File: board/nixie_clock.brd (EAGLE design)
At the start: 130 x 79 mm, 43 parts, among them U1 AMS1117-5.0, U2 SN74141N

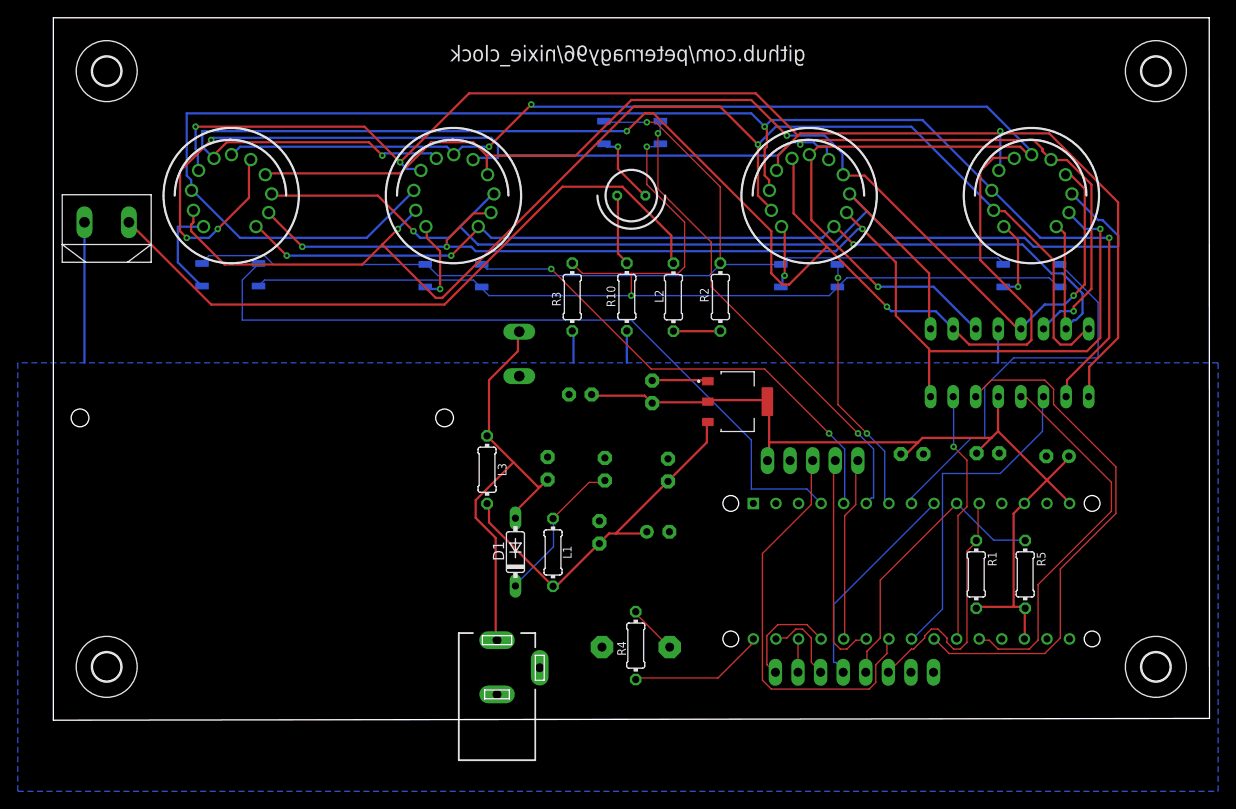
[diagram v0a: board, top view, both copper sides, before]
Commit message: D13 pin added and minor placement changes
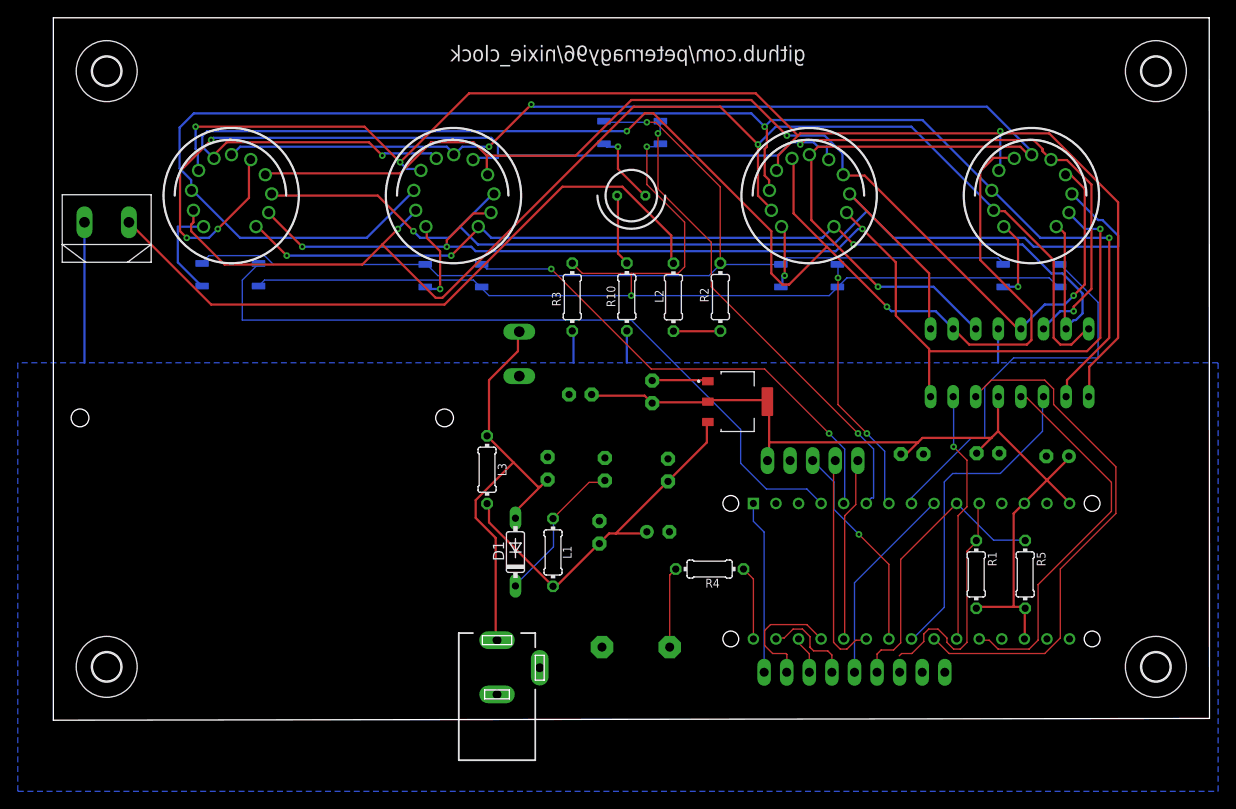
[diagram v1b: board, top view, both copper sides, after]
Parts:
- BUTTONS: device con-lstb:MA08-1 -> con-lstb:MA09-1
- moved R4 12.0 mm to (73.8, 17.0), turned to 180 degrees
- renumbered ARDUINO_NANO1 to ARDUINO_NANO
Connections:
- new net D13: ARDUINO_NANO.1, BUTTONS.9
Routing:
- net N$7: track 46.0 -> 24.1 mm, vias 0 -> 1
- net D13: track 0.00 -> 19.5 mm
- net N$8: track 15.5 -> 8.32 mm
- net D12: track 5.58 -> 9.06 mm
- net N$20: track 11.8 -> 13.9 mm
- net N$17: track 24.4 -> 22.7 mm
- net N$10: track 28.8 -> 27.2 mm
- net N$18: track 9.11 -> 10.6 mm
- net N$15: track 84.0 -> 83.0 mm
- net N$14: track 37.3 -> 36.6 mm
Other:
- board text added: "A5"
- board text added: "A6"
- board text added: "A7"
- board text added: "D10"
- board text added: "D11"
- board text added: "D13"
- board text added: "D9"
- board text removed: "b1"
- board text removed: "e"
- board text removed: "s1d"
- board text removed: "s1u"
- board text removed: "s2d"
- board text removed: "s2u"

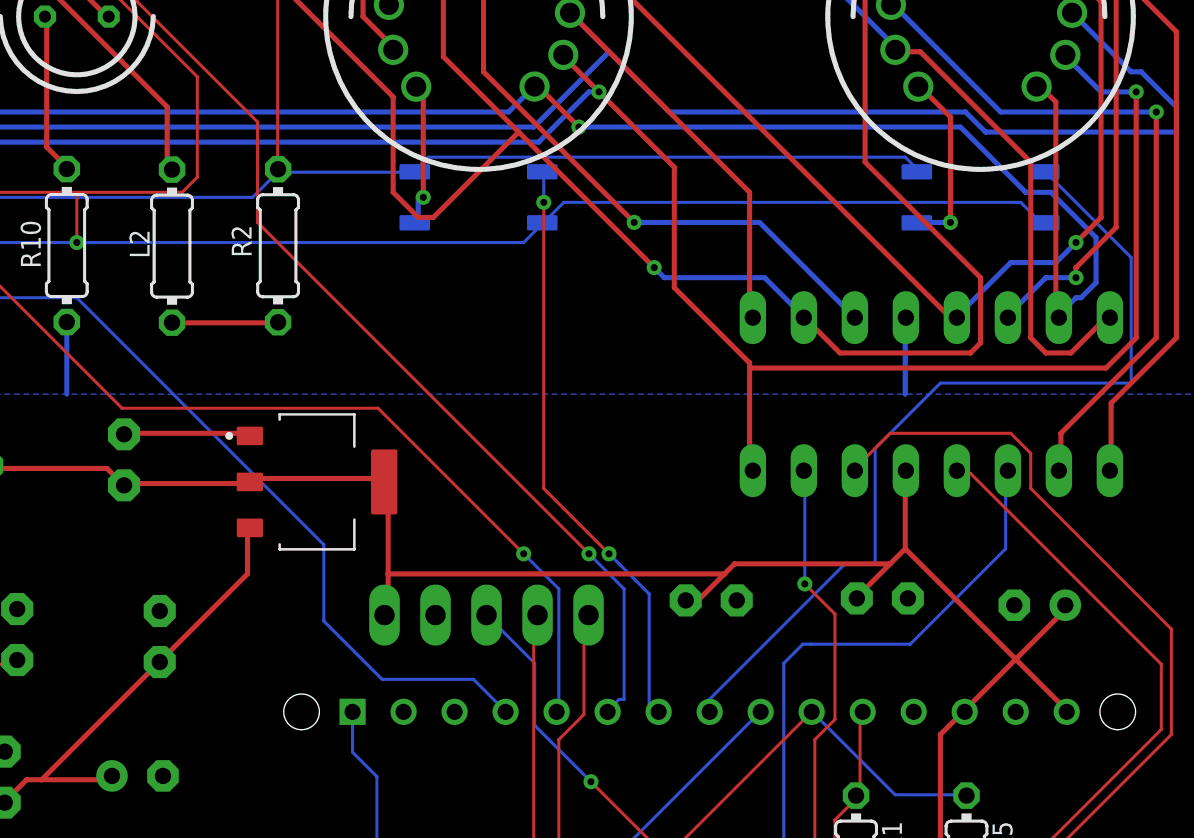
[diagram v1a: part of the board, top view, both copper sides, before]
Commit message: Diode before Arduino's VIN added
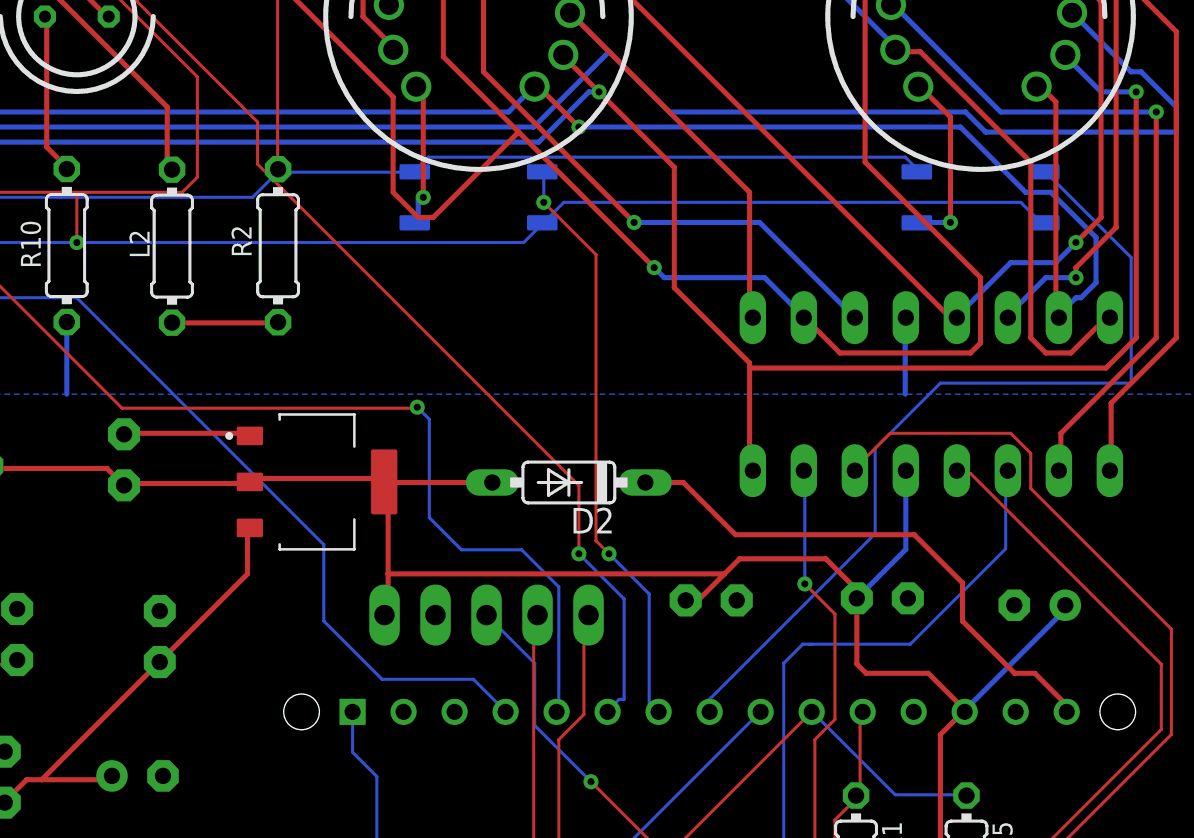
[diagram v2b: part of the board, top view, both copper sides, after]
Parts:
- added D2: 1N4148DO35-7, diode:DO35-7
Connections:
- new net N$1: ARDUINO_NANO.15, D2.C
- net +5V: now also D2.A; no longer ARDUINO_NANO.15
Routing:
- net N$1: track 0.00 -> 27.0 mm
- net N$26: track 55.6 -> 58.6 mm
- net +5V: track 102.5 -> 105.4 mm, vias 0 -> 1
- net N$29: track 43.9 -> 43.0 mm
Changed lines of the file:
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@@
 <attribute name="VALUE" x="108.8174" y="18.0256" size="0.9906" layer="27" ratio="10" rot="R270"/>
+</element>
+<element name="D2" library="diode" library_urn="urn:adsk.eagle:library:210" package="DO35-7" package3d_urn="urn:adsk.eagle:package:43339/2" value="1N4148DO35-7" x="89.5" y="35.8" smashed="yes" rot="R180">
+<attribute name="NAME" x="91.786" y="34.53" size="1.27" layer="25" ratio="10" rot="R180"/>
+<attribute name="POPULARITY" value="58" x="89.5" y="35.8" size="1.778" layer="27" rot="R180" display="off"/>
+<attribute name="VALUE" x="91.786" y="38.467" size="1.27" layer="27" ratio="10" rot="R180"/>
 </element>
 </elements>
@@
 <contactref element="C5" pad="+"/>
 <contactref element="C4" pad="1"/>
-<contactref element="ARDUINO_NANO" pad="15"/>
-<contactref element="ARDUINO_NANO" pad="13"/>
 <contactref element="C7" pad="1"/>
 <contactref element="RTC" pad="5"/>
@@
 <wire x1="80.25" y1="36" x2="80.305" y2="35.83" width="0.254" layer="1"/>
 <wire x1="73.75" y1="36" x2="73.615" y2="35.83" width="0.254" layer="1"/>
-<wire x1="106.25" y1="32.5" x2="106.25" y2="36.25" width="0.254" layer="1"/>
-<wire x1="104" y1="30.25" x2="105.5" y2="31.75" width="0.254" layer="1"/>
-<wire x1="105.5" y1="31.75" x2="106.25" y2="32.5" width="0.254" layer="1"/>
 <wire x1="106.25" y1="36.25" x2="106.28" y2="36.39" width="0.254" layer="1"/>
-<wire x1="104" y1="30.25" x2="103.84" y2="30.03" width="0.254" layer="1"/>
 <wire x1="96" y1="30" x2="95.5" y2="30" width="0.254" layer="1"/>
-<wire x1="97.75" y1="31.75" x2="97.25" y2="31.25" width="0.254" layer="1"/>
 <wire x1="97.25" y1="31.25" x2="96" y2="30" width="0.254" layer="1"/>
-<wire x1="105.5" y1="31.75" x2="97.75" y2="31.75" width="0.254" layer="1"/>
 <wire x1="95.5" y1="30" x2="95.32" y2="29.93" width="0.254" layer="1"/>
 <wire x1="109.25" y1="12.5" x2="109.25" y2="9.25" width="0.254" layer="1"/>
@@
 <wire x1="104" y1="12.75" x2="103.8" y2="12.59" width="0.254" layer="1"/>
 <wire x1="109.25" y1="12.75" x2="109.3" y2="12.59" width="0.254" layer="1"/>
-<wire x1="114.25" y1="29.5" x2="111.75" y2="27" width="0.254" layer="1"/>
-<wire x1="111.75" y1="27" x2="109.25" y2="24.5" width="0.254" layer="1"/>
-<wire x1="109.25" y1="24.5" x2="109.21" y2="24.38" width="0.254" layer="1"/>
+<wire x1="114.25" y1="29.5" x2="109.25" y2="24.5" width="0.254" layer="16"/>
 <wire x1="114.25" y1="29.5" x2="114.22" y2="29.69" width="0.254" layer="1"/>
-<wire x1="111.75" y1="27" x2="114.25" y2="24.5" width="0.254" layer="1"/>
-<wire x1="114.25" y1="24.5" x2="114.29" y2="24.38" width="0.254" layer="1"/>
 <wire x1="108" y1="23.25" x2="108" y2="12.75" width="0.254" layer="1"/>
 <wire x1="109" y1="24.25" x2="108" y2="23.25" width="0.254" layer="1"/>
-<wire x1="109" y1="24.25" x2="109.21" y2="24.38" width="0.254" layer="1"/>
-<wire x1="111.75" y1="27" x2="106.25" y2="32.5" width="0.254" layer="1"/>
 <wire x1="97.25" y1="31.25" x2="80.5" y2="31.25" width="0.254" layer="1"/>
+<contactref element="D2" pad="A"/>
+<wire x1="85.69" y1="35.8" x2="80.335" y2="35.8" width="0.254" layer="1"/>
+<wire x1="80.335" y1="35.8" x2="80.305" y2="35.83" width="0.254" layer="1"/>
+<contactref element="ARDUINO_NANO" pad="13"/>
+<via x="114.25" y="29.5" extent="1-16" drill="0.35"/>
+<wire x1="103.84" y1="30.03" x2="106.28" y2="32.47" width="0.254" layer="16"/>
+<wire x1="106.28" y1="32.47" x2="106.28" y2="36.39" width="0.254" layer="16"/>
+<wire x1="98" y1="32" x2="102.3" y2="32" width="0.254" layer="1"/>
+<wire x1="102.3" y1="32" x2="103.84" y2="30.46" width="0.254" layer="1"/>
+<wire x1="103.84" y1="30.46" x2="103.84" y2="30.03" width="0.254" layer="1"/>
+<wire x1="97.25" y1="31.25" x2="98" y2="32" width="0.254" layer="1"/>
+<wire x1="103.84" y1="30.03" x2="103.84" y2="26.76" width="0.254" layer="1"/>
+<wire x1="104.3" y1="26.3" x2="107.4" y2="26.3" width="0.254" layer="1"/>
+<wire x1="107.4" y1="26.3" x2="109.21" y2="24.49" width="0.254" layer="1"/>
+<wire x1="109.21" y1="24.49" x2="109.21" y2="24.38" width="0.254" layer="1"/>
+<wire x1="103.84" y1="26.76" x2="104.3" y2="26.3" width="0.254" layer="1"/>
+<wire x1="109.21" y1="24.38" x2="109.25" y2="24.5" width="0" layer="19" extent="16-16"/>
+<wire x1="109" y1="24.25" x2="109.21" y2="24.38" width="0" layer="19" extent="1-1"/>
 </signal>
 <signal name="200V" class="1">
@@
 <wire x1="56" y1="50.75" x2="48.75" y2="50.75" width="0.1524" layer="16"/>
 <wire x1="67.25" y1="39.5" x2="56" y2="50.75" width="0.1524" layer="1"/>
-<wire x1="80" y1="39.5" x2="67.25" y2="39.5" width="0.1524" layer="1"/>
-<wire x1="87.25" y1="32.25" x2="80" y2="39.5" width="0.1524" layer="1"/>
-<wire x1="89" y1="30.5" x2="87.25" y2="32.25" width="0.1524" layer="16"/>
-<wire x1="89" y1="24.5" x2="89" y2="30.5" width="0.1524" layer="16"/>
+<wire x1="81.95" y1="39.55" x2="81.9" y2="39.5" width="0.1524" layer="1"/>
+<wire x1="81.9" y1="39.5" x2="67.25" y2="39.5" width="0.1524" layer="1"/>
+<wire x1="89" y1="30.6" x2="87.15" y2="32.45" width="0.1524" layer="16"/>
+<wire x1="87.15" y1="32.45" x2="84.15" y2="32.45" width="0.1524" layer="16"/>
+<wire x1="84.15" y1="32.45" x2="82.55" y2="34.05" width="0.1524" layer="16"/>
+<wire x1="82.55" y1="38.95" x2="81.95" y2="39.55" width="0.1524" layer="16"/>
+<wire x1="82.55" y1="38.95" x2="82.55" y2="34.05" width="0.1524" layer="16"/>
+<wire x1="89" y1="24.5" x2="89" y2="30.6" width="0.1524" layer="16"/>
 <wire x1="48.25" y1="51.25" x2="48.175" y2="51.27" width="0.1524" layer="16"/>
 <wire x1="89" y1="24.5" x2="88.89" y2="24.38" width="0.1524" layer="16"/>
 <via x="56" y="50.75" extent="1-16" drill="0.35"/>
-<via x="87.25" y="32.25" extent="1-16" drill="0.35"/>
+<via x="81.95" y="39.55" extent="1-16" drill="0.35"/>
 </signal>
 <signal name="N$27">
@@
 <wire x1="68" y1="59.75" x2="68" y2="66" width="0.1524" layer="1"/>
 <wire x1="74" y1="53.75" x2="68" y2="59.75" width="0.1524" layer="1"/>
-<wire x1="74" y1="48.75" x2="74" y2="53.75" width="0.1524" layer="1"/>
-<wire x1="90.5" y1="32.25" x2="74" y2="48.75" width="0.1524" layer="1"/>
-<wire x1="92.25" y1="30.5" x2="90.5" y2="32.25" width="0.1524" layer="16"/>
-<wire x1="92.25" y1="25" x2="92.25" y2="30.5" width="0.1524" layer="16"/>
+<wire x1="74" y1="51.65" x2="74" y2="53.75" width="0.1524" layer="1"/>
+<wire x1="90" y1="32.25" x2="90" y2="35.65" width="0.1524" layer="1"/>
+<wire x1="90" y1="35.65" x2="74" y2="51.65" width="0.1524" layer="1"/>
+<wire x1="92.25" y1="30" x2="90" y2="32.25" width="0.1524" layer="16"/>
+<wire x1="92.25" y1="25" x2="92.25" y2="30" width="0.1524" layer="16"/>
 <wire x1="92" y1="25" x2="92.25" y2="25" width="0.1524" layer="16"/>
 <wire x1="91.5" y1="24.5" x2="92" y2="25" width="0.1524" layer="16"/>
@@
 <wire x1="91.5" y1="24.5" x2="91.43" y2="24.38" width="0.1524" layer="16"/>
 <via x="68" y="66" extent="1-16" drill="0.35"/>
-<via x="90.5" y="32.25" extent="1-16" drill="0.35"/>
+<via x="90" y="32.25" extent="1-16" drill="0.35"/>
 </signal>
 <signal name="N$28">
@@
 <contactref element="10MIN" pad="1"/>
 <wire x1="88.25" y1="49.75" x2="88.25" y2="51.25" width="0.1524" layer="16"/>
-<wire x1="88.25" y1="35.5" x2="88.25" y2="49.75" width="0.1524" layer="1"/>
-<wire x1="91.5" y1="32.25" x2="88.25" y2="35.5" width="0.1524" layer="1"/>
+<wire x1="90.85" y1="47.15" x2="88.25" y2="49.75" width="0.1524" layer="1"/>
+<wire x1="90.85" y1="47.15" x2="90.85" y2="32.9" width="0.1524" layer="1"/>
+<wire x1="91.5" y1="32.25" x2="90.85" y2="32.9" width="0.1524" layer="1"/>
 <wire x1="93.5" y1="30.25" x2="91.5" y2="32.25" width="0.1524" layer="16"/>
 <wire x1="93.5" y1="24.5" x2="93.5" y2="30.25" width="0.1524" layer="16"/>
@@
 <wire x1="117.5" y1="40.75" x2="117.5" y2="47" width="0.1524" layer="16"/>
 <wire x1="108" y1="40.75" x2="117.5" y2="40.75" width="0.1524" layer="16"/>
-<wire x1="104.75" y1="37.5" x2="108" y2="40.75" width="0.1524" layer="16"/>
-<wire x1="104.75" y1="31.75" x2="104.75" y2="37.5" width="0.1524" layer="16"/>
-<wire x1="103.25" y1="31.75" x2="104.75" y2="31.75" width="0.1524" layer="16"/>
-<wire x1="96.5" y1="25" x2="103.25" y2="31.75" width="0.1524" layer="16"/>
-<wire x1="96.5" y1="24.5" x2="96.5" y2="25" width="0.1524" layer="16"/>
+<wire x1="108" y1="40.75" x2="104.75" y2="37.5" width="0.1524" layer="16"/>
+<wire x1="96.5" y1="25" x2="96.5" y2="24.5" width="0.1524" layer="16"/>
 <wire x1="113.25" y1="51.25" x2="113.175" y2="51.27" width="0.1524" layer="16"/>
 <wire x1="96.5" y1="24.5" x2="96.51" y2="24.38" width="0.1524" layer="16"/>
+<wire x1="104.75" y1="37.5" x2="104.75" y2="33.25" width="0.1524" layer="16"/>
+<wire x1="104.75" y1="33.25" x2="96.5" y2="25" width="0.1524" layer="16"/>
 </signal>
 <signal name="K1" class="1">
@@
 <wire x1="79.94" y1="21.16" x2="78.73" y2="22.37" width="0.1524" layer="16"/>
 </signal>
+<signal name="N$1" class="1">
+<contactref element="ARDUINO_NANO" pad="15"/>
+<contactref element="D2" pad="C"/>
+<wire x1="95.2" y1="35.8" x2="97.8" y2="33.2" width="0.254" layer="1"/>
+<wire x1="97.8" y1="33.2" x2="106.7" y2="33.2" width="0.254" layer="1"/>
+<wire x1="93.31" y1="35.8" x2="95.2" y2="35.8" width="0.254" layer="1"/>
+<wire x1="106.7" y1="33.2" x2="109.1" y2="30.8" width="0.254" layer="1"/>
+<wire x1="109.1" y1="30.8" x2="109.1" y2="28.9" width="0.254" layer="1"/>
+<wire x1="109.1" y1="28.9" x2="111.7" y2="26.3" width="0.254" layer="1"/>
+<wire x1="111.7" y1="26.3" x2="112.7" y2="26.3" width="0.254" layer="1"/>
+<wire x1="112.7" y1="26.3" x2="114.29" y2="24.71" width="0.254" layer="1"/>
+<wire x1="114.29" y1="24.71" x2="114.29" y2="24.38" width="0.254" layer="1"/>
+</signal>
 </signals>

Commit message: board design v3
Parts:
- removed RTC: (no value), con-lstb:MA05-1
- added Q1: BC546B, transistor-npn:TO92-EBC
- added SV1: (no value), con-lstb:MA04-1
- moved BUTTONS 5.00 mm to (95.1, 5.49)
- flipped 12V to the top
- flipped 12V_INPUT to the bottom
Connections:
- removed net D12: BUZZER.+, R4.2
- removed net N$17: ARDUINO_NANO.9, BUTTONS.5
- removed net N$29: 1MIN.1, ARDUINO_NANO.8
- removed net N$8: ARDUINO_NANO.30, R4.1
- new net BUZ_IN: BUZZER.+, Q1.E
- new net BUZ_SGN: ARDUINO_NANO.30, Q1.B
- new net SCL: ARDUINO_NANO.9, SV1.1
- new net SDA: ARDUINO_NANO.8, SV1.2
- net +5V: now also SV1.3; no longer RTC.5
- net GND: now also SV1.4; no longer RTC.4
- net N$3: now also 1MIN.1, ARDUINO_NANO.24; no longer ARDUINO_NANO.26, RTC.1
- net N$4: now also BUTTONS.5; no longer RTC.2
- net N$7: now also Q1.C, R4.2; no longer ARDUINO_NANO.24, RTC.3
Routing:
- net N$27: track 53.8 -> 124.8 mm, vias 2 -> 1
- net K9: track 176.2 -> 232.2 mm, vias 2 -> 3
- net N$29: track 43.0 -> 0.00 mm
- net K7: track 179.1 -> 136.6 mm, vias 3 -> 5
- net K0: track 149.3 -> 191.0 mm, vias 2 -> 1
- net N$3: track 20.7 -> 61.8 mm, vias 0 -> 1
- net N$12: track 28.4 -> 58.7 mm, vias 1 -> 0
- net N$13: track 59.1 -> 30.4 mm
- net K6: track 152.7 -> 126.1 mm
- net N$14: track 36.6 -> 61.6 mm
- net N$17: track 22.7 -> 0.00 mm
- net SCL: track 0.00 -> 21.9 mm
- net N$4: track 25.0 -> 5.21 mm
- net N$16: track 125.3 -> 144.1 mm
- net SDA: track 0.00 -> 15.3 mm
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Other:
- board text added: "D7"
- board text removed: "A5"
